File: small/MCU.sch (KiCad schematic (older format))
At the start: 35 parts, among them IC1 PIC32MX350F256H-V_PT, J3 Micro_SD_Card, J4 Conn_01x05_Female, U5 AT25M02, U8 PCF8563T, Y2 Crystal

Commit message: ENC28j60 package changed to soic 28 17.9
TODO: route
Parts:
- C25: Price (none) -> 0.1662
- IC1, J3, J4, TP1, TP2, TP3, TP4, TP5, TP6, TP7, TP8: LCSC (none) -> N/A
- R24: LCSC C7250 -> C7250
- R6: LCSC C21190 -> C21190
- U5: LCSC - -> N/A
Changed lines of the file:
@@
 F 2 "Resistor_SMD:R_0603_1608Metric" V 1730 3450 50  0001 C CNN
 F 3 "https://eu.mouser.com/datasheet/2/427/crcwce3-1762584.pdf" H 1800 3450 50  0001 C CNN
-F 4 " C21190" H 1800 3450 50  0001 C CNN "LCSC"
+F 4 "C21190" H 1800 3450 50  0001 C CNN "LCSC"
 F 5 "0.009" H 1800 3450 50  0001 C CNN "Price"
 F 6 "0603WAF1001T5E" H 1800 3450 50  0001 C CNN "MPN"
@@
 F 3 "~" H 10575 875 50  0001 C CNN
 F 4 "Connector unknown" H 10575 875 50  0001 C CNN "Mpn"
+F 5 "N/A" H 10575 875 50  0001 C CNN "LCSC"
 	1    10575 875
 	0    -1   -1   0
@@
 F 2 "Connector_Card:microSD_HC_Hirose_DM3BT-DSF-PEJS" H 11200 3050 50  0001 C CNN
 F 3 "http://katalog.we-online.de/em/datasheet/693072010801.pdf" H 10050 2750 50  0001 C CNN
+F 4 "N/A" H 10050 2750 50  0001 C CNN "LCSC"
 	1    10050 2750
 	1    0    0    -1
@@
 F 2 "Package_SO:SOIC-8_3.9x4.9mm_P1.27mm" H 1650 7150 50  0001 C CNN
 F 3 "http://ww1.microchip.com/downloads/en/DeviceDoc/Atmel-8707-SEEPROM-AT25010B-020B-040B-Datasheet.pdf" H 1650 7150 50  0001 C CNN
-F 4 "-" H 1650 7150 50  0001 C CNN "LCSC"
+F 4 "N/A" H 1650 7150 50  0001 C CNN "LCSC"
 F 5 "AT25M02-SSHD-T" H 1650 7150 50  0001 C CNN "MPN"
 F 6 "2.60" H 1650 7150 50  0001 C CNN "Price"
@@
 F 2 "Resistor_SMD:R_0603_1608Metric" V 9655 4750 50  0001 C CNN
 F 3 "~" H 9725 4750 50  0001 C CNN
-F 4 " C7250" V 9725 4750 50  0001 C CNN "LCSC"
+F 4 "C7250" V 9725 4750 50  0001 C CNN "LCSC"
 F 5 "0603WAF1005T5E" H 9725 4750 50  0001 C CNN "MPN"
 F 6 "0.0028" H 9725 4750 50  0001 C CNN "Price"
@@
 F 2 "TestPoint:TestPoint_Pad_1.5x1.5mm" H 5300 7400 50  0001 C CNN
 F 3 "~" H 5300 7400 50  0001 C CNN
+F 4 "N/A" H 5100 7400 50  0001 C CNN "LCSC"
 	1    5100 7400
 	-1   0    0    1
@@
 F 2 "TestPoint:TestPoint_Pad_1.5x1.5mm" H 5400 7400 50  0001 C CNN
 F 3 "~" H 5400 7400 50  0001 C CNN
+F 4 "N/A" H 5200 7400 50  0001 C CNN "LCSC"
 	1    5200 7400
 	-1   0    0    1
@@
 F 2 "TestPoint:TestPoint_Pad_1.5x1.5mm" H 5700 7400 50  0001 C CNN
 F 3 "~" H 5700 7400 50  0001 C CNN
+F 4 "N/A" H 5500 7400 50  0001 C CNN "LCSC"
 	1    5500 7400
 	-1   0    0    1
@@
 F 2 "TestPoint:TestPoint_Pad_1.5x1.5mm" H 4900 1450 50  0001 C CNN
 F 3 "~" H 4900 1450 50  0001 C CNN
+F 4 "N/A" H 4700 1450 50  0001 C CNN "LCSC"
 	1    4700 1450
 	1    0    0    -1
@@
 F 2 "TestPoint:TestPoint_Pad_1.5x1.5mm" H 3925 7175 50  0001 C CNN
 F 3 "~" H 3925 7175 50  0001 C CNN
+F 4 "N/A" H 3725 7175 50  0001 C CNN "LCSC"
 	1    3725 7175
 	-1   0    0    1
@@
 F 2 "TestPoint:TestPoint_Pad_1.5x1.5mm" H 4125 7175 50  0001 C CNN
 F 3 "~" H 4125 7175 50  0001 C CNN
+F 4 "N/A" H 3925 7175 50  0001 C CNN "LCSC"
 	1    3925 7175
 	-1   0    0    1
@@
 F 11 "https://www.arrow.com/en/products/pic32mx350f256h-vpt/microchip-technology" H 6950 3150 50  0001 L CNN "Arrow Price/Stock"
 F 12 "PIC32MX350F256H-V/PT" H 3400 2850 50  0001 C CNN "MPN"
+F 13 "N/A" H 3400 2850 50  0001 C CNN "LCSC"
 	1    3400 2850
 	1    0    0    -1
@@
 F 2 "TestPoint:TestPoint_Pad_1.5x1.5mm" H 4800 6850 50  0001 C CNN
 F 3 "~" H 4800 6850 50  0001 C CNN
+F 4 "N/A" H 4600 6850 50  0001 C CNN "LCSC"
 	1    4600 6850
 	-1   0    0    1
@@
 F 2 "TestPoint:TestPoint_Pad_1.5x1.5mm" H 4700 6850 50  0001 C CNN
 F 3 "~" H 4700 6850 50  0001 C CNN
+F 4 "N/A" H 4500 6850 50  0001 C CNN "LCSC"
 	1    4500 6850
 	-1   0    0    1
@@
 F 5 "C38065" H 8950 4250 50  0001 C CNN "LCSC"
 F 6 "XH414HG-IV01E" H 8950 4250 50  0001 C CNN "MPN"
+F 7 "0.1662" H 8950 4250 50  0001 C CNN "Price"
 	1    8950 4250
 	1    0    0    -1

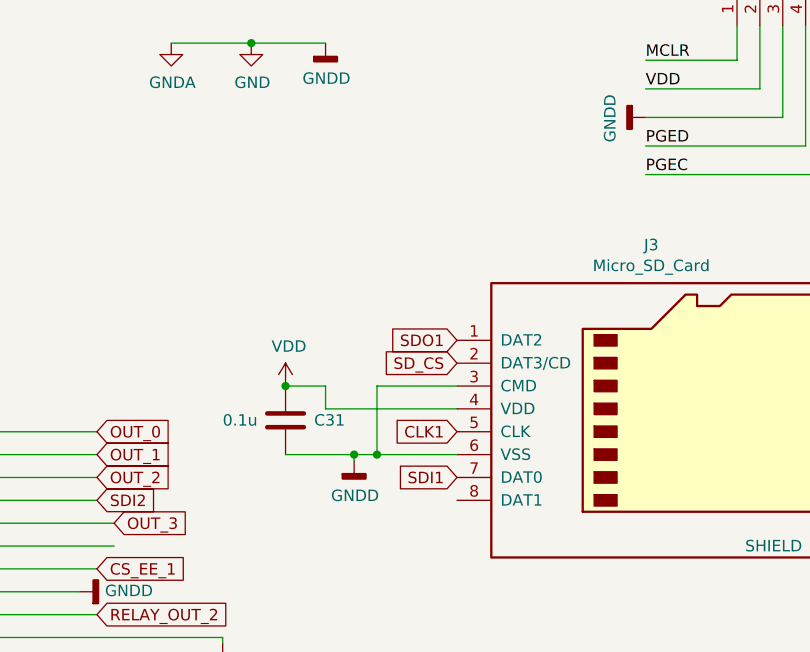
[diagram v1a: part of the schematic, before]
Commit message: SPI change:
ENC28j60 on one spi
SDCARD and EEPROM on the other.
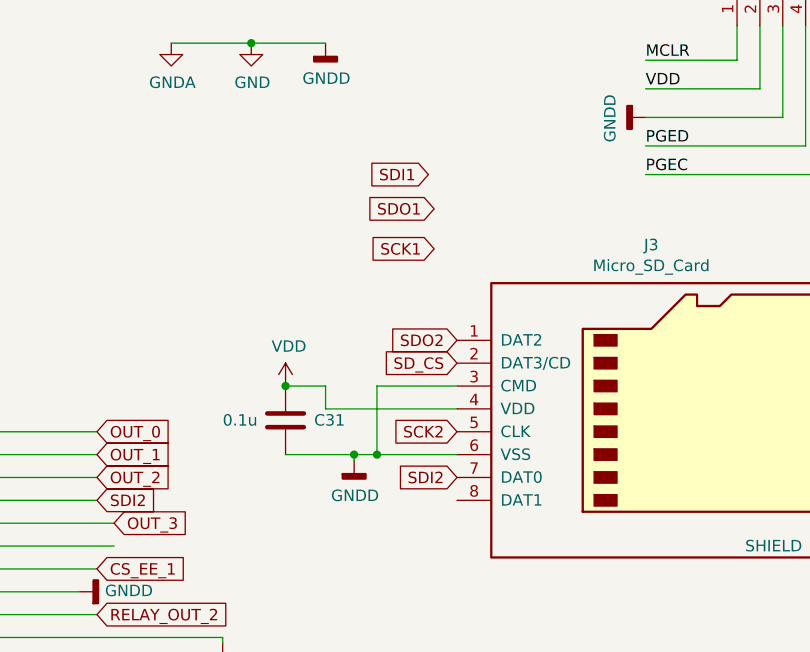
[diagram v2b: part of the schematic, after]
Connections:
- net CLK1 is gone; now on net SCK2: J3.5 (CLK)
- net SDI1: no longer J3.7 (DAT0)
- net SDI2: now also J3.7 (DAT0)
- net SDO1: no longer J3.1 (DAT2)
- net SDO2: now also J3.1 (DAT2)
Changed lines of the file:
@@
 Text GLabel 9150 2550 0    50   Input ~ 0
 SD_CS
-Text GLabel 9150 2450 0    50   Input ~ 0
-SDO1
-Text GLabel 9150 2850 0    50   Input ~ 0
-CLK1
-Text GLabel 9150 3050 0    50   Input ~ 0
-SDI1
 Wire Wire Line
 	9150 2950 8800 2950
@@
 Wire Wire Line
 	9525 4600 9525 4750
+Text GLabel 9150 2450 0    50   Input ~ 0
+SDO2
+Text GLabel 9150 2850 0    50   Input ~ 0
+SCK2
+Text GLabel 9050 1875 0    50   Input ~ 0
+SDO1
+Text GLabel 9050 2050 0    50   Input ~ 0
+SCK1
+Text GLabel 9025 1725 0    50   Input ~ 0
+SDI1
+Text GLabel 9150 3050 0    50   Input ~ 0
+SDI2
 $EndSCHEMATC

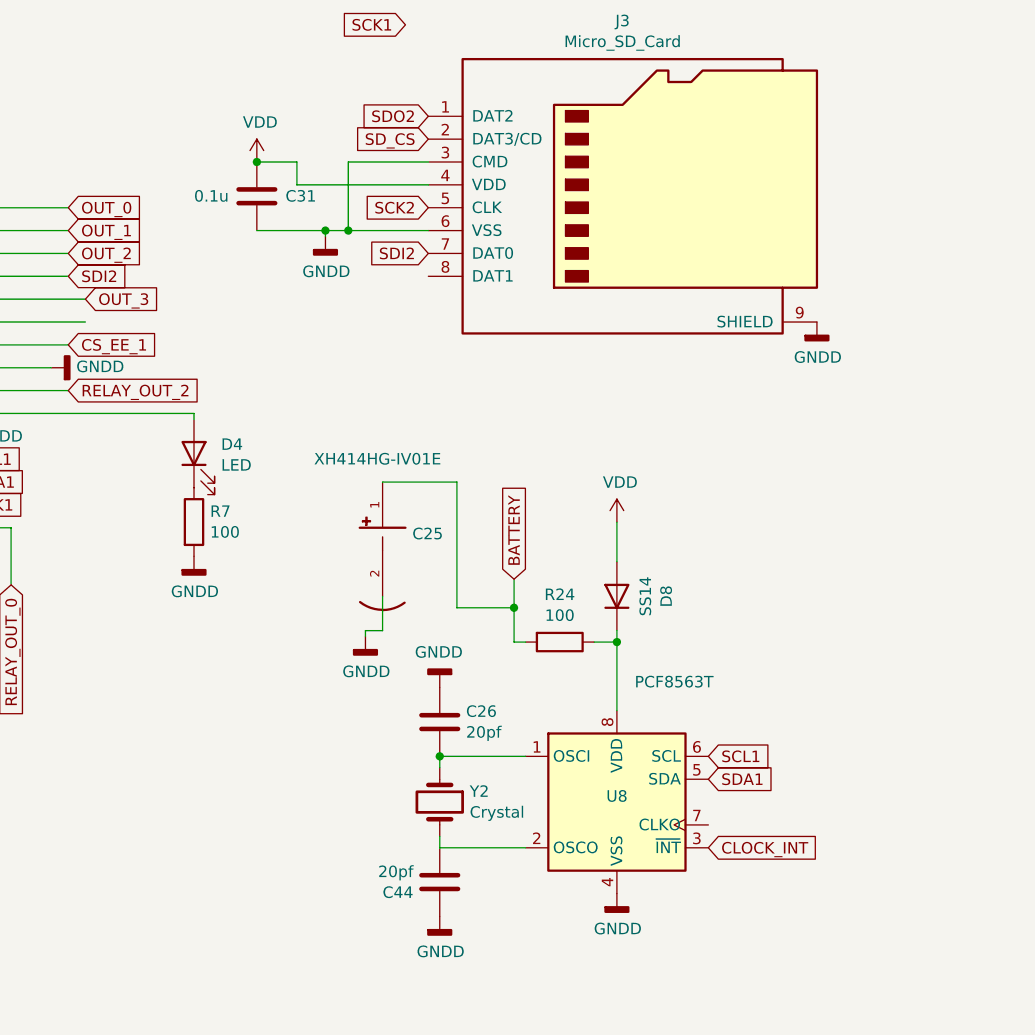
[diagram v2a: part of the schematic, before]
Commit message: sdcard and clock capacitor added.
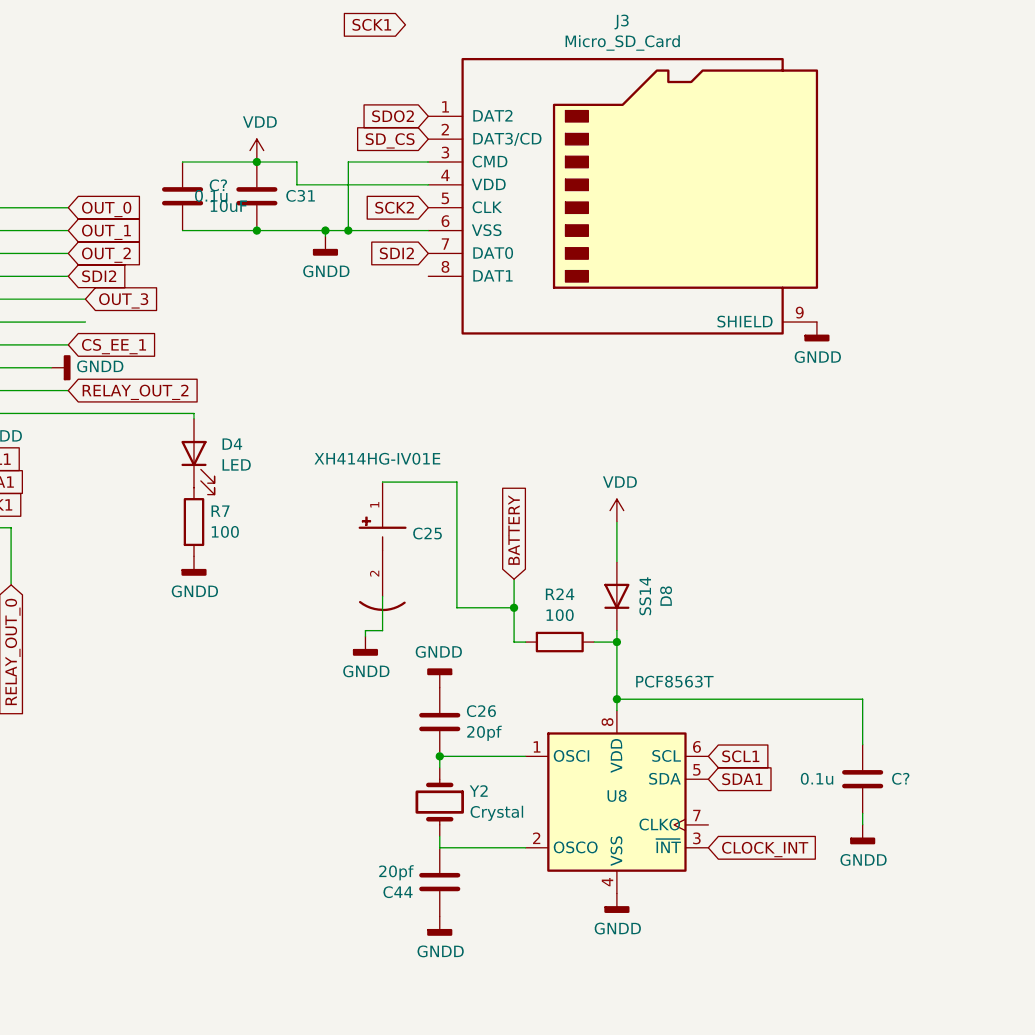
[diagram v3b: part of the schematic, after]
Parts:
- added C?: 10uF, Capacitor_SMD:C_1206_3216Metric, symbol Device:C
- added C?: 0.1u, Capacitor_SMD:C_0603_1608Metric, symbol Device:C
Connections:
- net GND: now also C?.2, C?.2
- net VDD: now also C?.1
- net at D8.2 (K), R24.1, U8.8 (VDD): now also C?.1
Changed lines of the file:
@@
 Connection ~ 9975 4750
 Wire Wire Line
-	9975 4750 9975 5050
+	9975 4750 9975 5000
 $Comp
 L Device:R R24
@@
 	1    0    0    -1
 $EndComp
-Wire Wire Line
-	8400 2950 8700 2950
 Connection ~ 8700 2950
 Wire Wire Line
@@
 Text GLabel 9150 3050 0    50   Input ~ 0
 SDI2
+$Comp
+L Device:C C?
+U 1 1 6032E617
+P 8075 2800
+F 0 "C?" H 8190 2846 50  0000 L CNN
+F 1 "10uF" H 8190 2755 50  0000 L CNN
+F 2 "Capacitor_SMD:C_1206_3216Metric" H 8113 2650 50  0001 C CNN
+F 3 "https://datasheet.lcsc.com/szlcsc/Samsung-Electro-Mechanics-CL31A106KBHNNNE_C13585.pdf" H 8075 2800 50  0001 C CNN
+F 4 "C13585" H 8075 2800 50  0001 C CNN "LCSC"
+F 5 "CL31A106KBHNNNE" H 8075 2800 50  0001 C CNN "MPN"
+F 6 "0" H 8075 2800 50  0001 C CNN "source"
+F 7 "0.0549" H 8075 2800 50  0001 C CNN "Price"
+	1    8075 2800
+	1    0    0    -1
+$EndComp
+Wire Wire Line
+	8075 2950 8400 2950
+Connection ~ 8400 2950
+Wire Wire Line
+	8400 2950 8700 2950
+Wire Wire Line
+	8075 2650 8400 2650
+$Comp
+L Device:C C?
+U 1 1 6033E276
+P 11050 5350
+AR Path="/6033E276" Ref="C?"  Part="1"
+AR Path="/6078415F/6033E276" Ref="C?"  Part="1"
+F 0 "C?" H 11175 5350 50  0000 L CNN
+F 1 "0.1u" H 10775 5350 50  0000 L CNN
+F 2 "Capacitor_SMD:C_0603_1608Metric" H 11088 5200 50  0001 C CNN
+F 3 "https://datasheet.lcsc.com/szlcsc/YAGEO-CC0603KRX7R9BB104_C14663.pdf" H 11050 5350 50  0001 C CNN
+F 4 "C14663" H 11050 5350 50  0001 C CNN "LCSC"
+F 5 "0.0071" H 11050 5350 50  0001 C CNN "Price"
+F 6 "CC0603KRX7R9BB104" H 11050 5350 50  0001 C CNN "MPN"
+F 7 "0" H 11050 5350 50  0001 C CNN "source"
+	1    11050 5350
+	1    0    0    -1
+$EndComp
+Wire Wire Line
+	11050 5000 9975 5000
+Connection ~ 9975 5000
+Wire Wire Line
+	9975 5000 9975 5050
+Wire Wire Line
+	11050 5000 11050 5200
+$Comp
+L power:GNDD #PWR?
+U 1 1 60348076
+P 11050 5550
+F 0 "#PWR?" H 11050 5300 50  0001 C CNN
+F 1 "GNDD" H 11054 5395 50  0000 C CNN
+F 2 "" H 11050 5550 50  0001 C CNN
+F 3 "" H 11050 5550 50  0001 C CNN
+	1    11050 5550
+	1    0    0    -1
+$EndComp
+Wire Wire Line
+	11050 5500 11050 5550
 $EndSCHEMATC

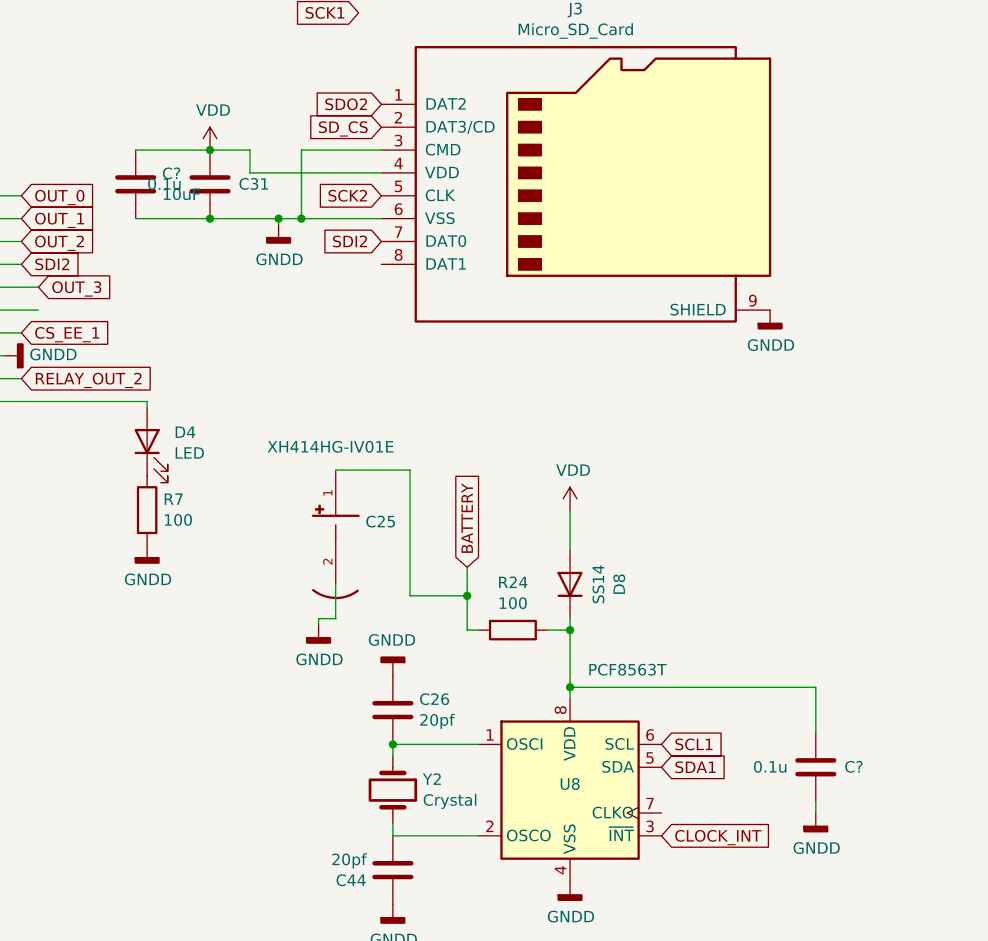
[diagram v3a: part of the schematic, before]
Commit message: 3.3V changed to basic part.
thermal vias added for 5V regulator
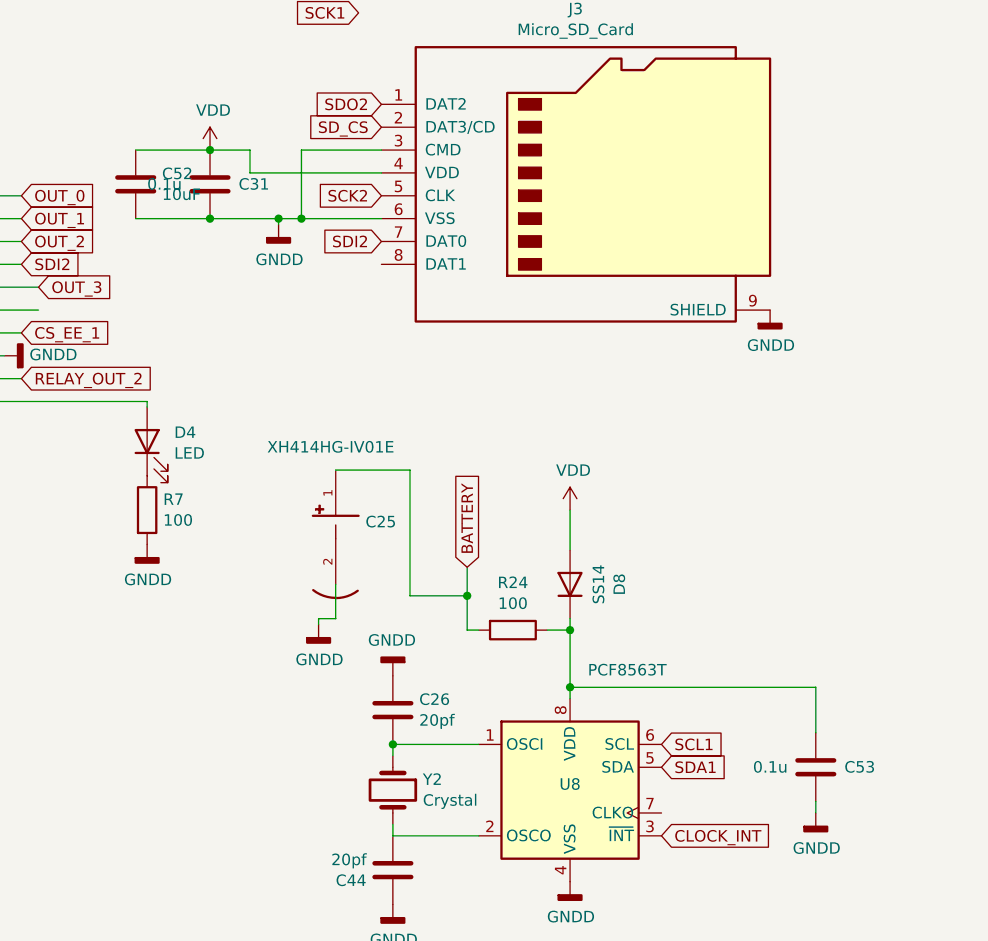
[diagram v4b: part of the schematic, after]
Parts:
- gave numbers to parts that had none: 2
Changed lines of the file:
@@
 U 1 1 6032E617
 P 8075 2800
-F 0 "C?" H 8190 2846 50  0000 L CNN
+AR Path="/6010B004/6032E617" Ref="C?"  Part="1"
+AR Path="/6078415F/6032E617" Ref="C52"  Part="1"
+F 0 "C52" H 8190 2846 50  0000 L CNN
 F 1 "10uF" H 8190 2755 50  0000 L CNN
 F 2 "Capacitor_SMD:C_1206_3216Metric" H 8113 2650 50  0001 C CNN
@@
 P 11050 5350
 AR Path="/6033E276" Ref="C?"  Part="1"
-AR Path="/6078415F/6033E276" Ref="C?"  Part="1"
-F 0 "C?" H 11175 5350 50  0000 L CNN
+AR Path="/6078415F/6033E276" Ref="C53"  Part="1"
+F 0 "C53" H 11175 5350 50  0000 L CNN
 F 1 "0.1u" H 10775 5350 50  0000 L CNN
 F 2 "Capacitor_SMD:C_0603_1608Metric" H 11088 5200 50  0001 C CNN
@@
 	11050 5000 11050 5200
 $Comp
-L power:GNDD #PWR?
+L power:GNDD #PWR0169
 U 1 1 60348076
 P 11050 5550
-F 0 "#PWR?" H 11050 5300 50  0001 C CNN
+F 0 "#PWR0169" H 11050 5300 50  0001 C CNN
 F 1 "GNDD" H 11054 5395 50  0000 C CNN
 F 2 "" H 11050 5550 50  0001 C CNN

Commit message: fabrication output prepared
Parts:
- C25: footprint CAP_XH414HG-IV01E -> small:CAP_XH414HG-IV01E
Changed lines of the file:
@@
 F 0 "C25" H 9080 4223 50  0000 L CNN
 F 1 "XH414HG-IV01E" H 8650 4550 50  0000 L CNN
-F 2 "CAP_XH414HG-IV01E" H 8950 4250 50  0001 L BNN
+F 2 "small:CAP_XH414HG-IV01E" H 8950 4250 50  0001 L BNN
 F 3 "" H 8950 4250 50  0001 L BNN
 F 4 "Seiko" H 8950 4250 50  0001 L BNN "MANUFACTURER"
